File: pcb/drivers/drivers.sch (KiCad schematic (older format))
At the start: 19 parts, among them J1 Conn_01x04_Male, J2 Conn_01x04_Male, J3 Conn_01x04_Male, J4 Conn_01x04_Male, J5 Conn_01x04_Male, P1 Digital, P2 COM, P3 ADC, P4 Analog, P5 ADC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

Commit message: Polishing
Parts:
- added C2, C3: 0.1uF, Capacitor_SMD:C_0805_2012Metric_Pad1.18x1.45mm_HandSolder, symbol Device:C
- added J6: Conn_01x02_Male, TerminalBlock_Phoenix:TerminalBlock_Phoenix_MKDS-1,5-2_1x02_P5.00mm_Horizontal, symbol Connector:Conn_01x02_Male
- added Q5: IRLML6402, Package_TO_SOT_SMD:SOT-23, symbol Transistor_FET:IRLML6402
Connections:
- wire segments 81 -> 82
- no-connect marks 19 -> 18
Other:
- note added: "Power\n+5V"
- note added: "Reverse\npolarity\nprotection"
- moved on the sheet: C1
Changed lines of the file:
@@
 L Device:CP C1
 U 1 1 5FFF86DA
-P 7250 4175
-F 0 "C1" H 7368 4221 50  0000 L CNN
-F 1 "1000uF" H 7368 4130 50  0000 L CNN
-F 2 "Capacitor_THT:CP_Radial_D8.0mm_P2.50mm" H 7288 4025 50  0001 C CNN
-F 3 "~" H 7250 4175 50  0001 C CNN
-	1    7250 4175
+P 7000 5250
+F 0 "C1" H 7118 5296 50  0000 L CNN
+F 1 "1000uF" H 7118 5205 50  0000 L CNN
+F 2 "Capacitor_THT:CP_Radial_D8.0mm_P2.50mm" H 7038 5100 50  0001 C CNN
+F 3 "~" H 7000 5250 50  0001 C CNN
+	1    7000 5250
 	1    0    0    -1
 $EndComp
@@
 L power:GND #PWR016
 U 1 1 5FFF93FD
-P 7250 4325
-F 0 "#PWR016" H 7250 4075 50  0001 C CNN
-F 1 "GND" H 7255 4152 50  0000 C CNN
-F 2 "" H 7250 4325 50  0001 C CNN
-F 3 "" H 7250 4325 50  0001 C CNN
-	1    7250 4325
+P 7000 5400
+F 0 "#PWR016" H 7000 5150 50  0001 C CNN
+F 1 "GND" H 7005 5227 50  0000 C CNN
+F 2 "" H 7000 5400 50  0001 C CNN
+F 3 "" H 7000 5400 50  0001 C CNN
+	1    7000 5400
 	1    0    0    -1
 $EndComp
@@
 L power:VCC #PWR015
 U 1 1 5FFF9E1A
-P 7250 4025
-F 0 "#PWR015" H 7250 3875 50  0001 C CNN
-F 1 "VCC" H 7265 4198 50  0000 C CNN
-F 2 "" H 7250 4025 50  0001 C CNN
-F 3 "" H 7250 4025 50  0001 C CNN
-	1    7250 4025
+P 7000 5100
+F 0 "#PWR015" H 7000 4950 50  0001 C CNN
+F 1 "VCC" H 7015 5273 50  0000 C CNN
+F 2 "" H 7000 5100 50  0001 C CNN
+F 3 "" H 7000 5100 50  0001 C CNN
+	1    7000 5100
 	1    0    0    -1
 $EndComp
@@
 NoConn ~ 9000 2700
 NoConn ~ 9100 2300
-NoConn ~ 7600 3100
 NoConn ~ 9550 1000
 NoConn ~ 10350 1500
@@
 NoConn ~ 10050 3200
 NoConn ~ 9450 3225
+$Comp
+L Transistor_FET:IRLML6402 Q5
+U 1 1 5FF9B9AF
+P 7200 3850
+F 0 "Q5" V 7125 3900 50  0000 L CNN
+F 1 "IRLML6402" H 6850 3700 50  0000 L CNN
+F 2 "Package_TO_SOT_SMD:SOT-23" H 7400 3775 50  0001 L CIN
+F 3 "https://www.infineon.com/dgdl/irlml6402pbf.pdf?fileId=5546d462533600a401535668d5c2263c" H 7200 3850 50  0001 L CNN
+	1    7200 3850
+	0    -1   -1   0
+$EndComp
+$Comp
+L power:GND #PWR018
+U 1 1 5FFAC25B
+P 7200 4050
+F 0 "#PWR018" H 7200 3800 50  0001 C CNN
+F 1 "GND" H 7205 3877 50  0000 C CNN
+F 2 "" H 7200 4050 50  0001 C CNN
+F 3 "" H 7200 4050 50  0001 C CNN
+	1    7200 4050
+	1    0    0    -1
+$EndComp
+$Comp
+L Connector:Conn_01x02_Male J6
+U 1 1 5FFACF24
+P 6575 3750
+F 0 "J6" H 6683 3931 50  0000 C CNN
+F 1 "Conn_01x02_Male" H 6700 3475 50  0000 C CNN
+F 2 "TerminalBlock_Phoenix:TerminalBlock_Phoenix_MKDS-1,5-2_1x02_P5.00mm_Horizontal" H 6575 3750 50  0001 C CNN
+F 3 "~" H 6575 3750 50  0001 C CNN
+	1    6575 3750
+	1    0    0    -1
+$EndComp
+$Comp
+L power:GND #PWR017
+U 1 1 5FFADAD8
+P 6775 3850
+F 0 "#PWR017" H 6775 3600 50  0001 C CNN
+F 1 "GND" H 6900 3825 50  0000 C CNN
+F 2 "" H 6775 3850 50  0001 C CNN
+F 3 "" H 6775 3850 50  0001 C CNN
+	1    6775 3850
+	1    0    0    -1
+$EndComp
+Wire Wire Line
+	6775 3750 7000 3750
+Text Notes 6300 3875 0    50   ~ 0
+Power\n+5V
+Text Notes 7050 3550 0    50   ~ 0
+Reverse\npolarity\nprotection
+$Comp
+L power:VCC #PWR019
+U 1 1 5FFB386E
+P 7400 3750
+F 0 "#PWR019" H 7400 3600 50  0001 C CNN
+F 1 "VCC" V 7415 3878 50  0000 L CNN
+F 2 "" H 7400 3750 50  0001 C CNN
+F 3 "" H 7400 3750 50  0001 C CNN
+	1    7400 3750
+	0    1    1    0
+$EndComp
+$Comp
+L Device:C C2
+U 1 1 5FFF57D4
+P 7625 5250
+F 0 "C2" H 7740 5296 50  0000 L CNN
+F 1 "0.1uF" H 7740 5205 50  0000 L CNN
+F 2 "Capacitor_SMD:C_0805_2012Metric_Pad1.18x1.45mm_HandSolder" H 7663 5100 50  0001 C CNN
+F 3 "~" H 7625 5250 50  0001 C CNN
+	1    7625 5250
+	1    0    0    -1
+$EndComp
+$Comp
+L power:VCC #PWR020
+U 1 1 5FFF6495
+P 7625 5100
+F 0 "#PWR020" H 7625 4950 50  0001 C CNN
+F 1 "VCC" H 7640 5273 50  0000 C CNN
+F 2 "" H 7625 5100 50  0001 C CNN
+F 3 "" H 7625 5100 50  0001 C CNN
+	1    7625 5100
+	1    0    0    -1
+$EndComp
+$Comp
+L power:GND #PWR021
+U 1 1 5FFF6FB4
+P 7625 5400
+F 0 "#PWR021" H 7625 5150 50  0001 C CNN
+F 1 "GND" H 7630 5227 50  0000 C CNN
+F 2 "" H 7625 5400 50  0001 C CNN
+F 3 "" H 7625 5400 50  0001 C CNN
+	1    7625 5400
+	1    0    0    -1
+$EndComp
+$Comp
+L Device:C C3
+U 1 1 5FFF9188
+P 8250 5250
+F 0 "C3" H 8365 5296 50  0000 L CNN
+F 1 "0.1uF" H 8365 5205 50  0000 L CNN
+F 2 "Capacitor_SMD:C_0805_2012Metric_Pad1.18x1.45mm_HandSolder" H 8288 5100 50  0001 C CNN
+F 3 "~" H 8250 5250 50  0001 C CNN
+	1    8250 5250
+	1    0    0    -1
+$EndComp
+$Comp
+L power:VCC #PWR022
+U 1 1 5FFF918E
+P 8250 5100
+F 0 "#PWR022" H 8250 4950 50  0001 C CNN
+F 1 "VCC" H 8265 5273 50  0000 C CNN
+F 2 "" H 8250 5100 50  0001 C CNN
+F 3 "" H 8250 5100 50  0001 C CNN
+	1    8250 5100
+	1    0    0    -1
+$EndComp
+$Comp
+L power:GND #PWR023
+U 1 1 5FFF9194
+P 8250 5400
+F 0 "#PWR023" H 8250 5150 50  0001 C CNN
+F 1 "GND" H 8255 5227 50  0000 C CNN
+F 2 "" H 8250 5400 50  0001 C CNN
+F 3 "" H 8250 5400 50  0001 C CNN
+	1    8250 5400
+	1    0    0    -1
+$EndComp
 $EndSCHEMATC

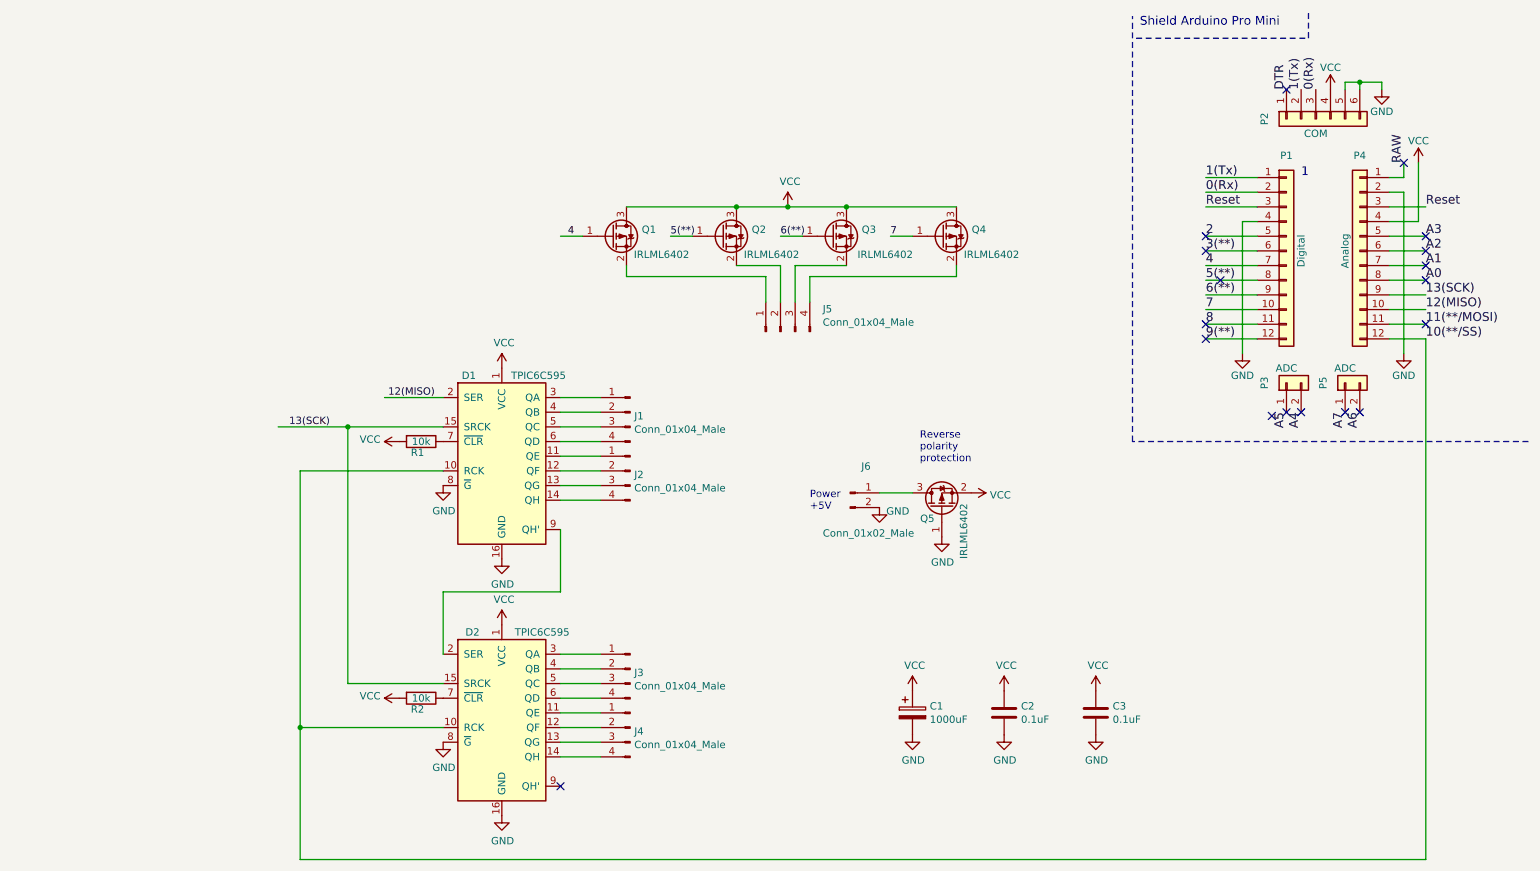
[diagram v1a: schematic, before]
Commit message: Replace Arduino Pro Mini to another Arduino Pro Mini
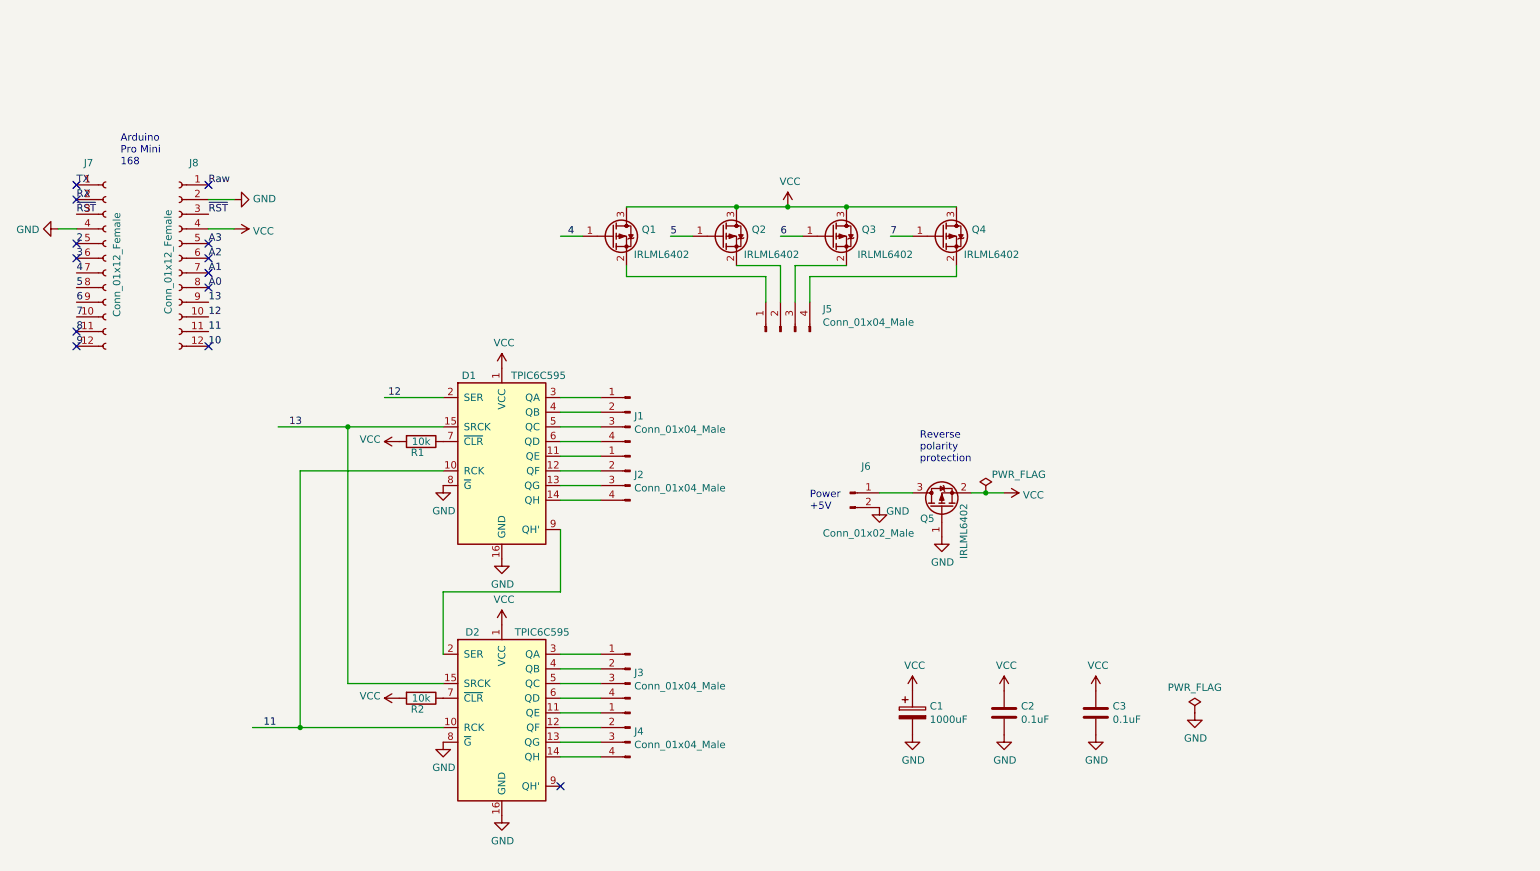
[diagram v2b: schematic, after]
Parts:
- removed P1: Digital, Socket_Arduino_Pro_Mini:Socket_Strip_Arduino_1x12, symbol Connector_Generic:Conn_01x12
- removed P2: COM, Socket_Arduino_Pro_Mini:Socket_Strip_Arduino_1x06, symbol Connector_Generic:Conn_01x06
- removed P3, P5: ADC, Socket_Arduino_Pro_Mini:Socket_Strip_Arduino_1x02, symbol Connector_Generic:Conn_01x02
- removed P4: Analog, Socket_Arduino_Pro_Mini:Socket_Strip_Arduino_1x12, symbol Connector_Generic:Conn_01x12
- added J7, J8: Conn_01x12_Female, Connector_PinSocket_2.54mm:PinSocket_1x12_P2.54mm_Vertical, symbol Connector:Conn_01x12_Female
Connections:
- net labels added: 10, 11, 12, 13, 3, 5, 6, 9, RX, Raw, TX, ~RST
- net labels removed: 0(Rx), 1(Tx), 10(**/SS), 11(**/MOSI), 12(MISO), 13(SCK), 3(**), 5(**), 6(**), 9(**), A4, A5, A6, A7, DTR, RAW, Reset
- wire segments 82 -> 52
- no-connect marks 18 -> 13
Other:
- note added: "Arduino\nPro Mini\n168"
- note removed: "1"
- note removed: "Shield Arduino Pro Mini \n"

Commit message: Swap pin 12 and 13
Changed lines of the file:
@@
 $EndComp
 Text Label 3425 3100 0    50   ~ 0
-12
+13
 Wire Wire Line
 	3800 3100 3400 3100
@@
 	3800 3300 3150 3300
 Text Label 2750 3300 0    50   ~ 0
-13
+12
 Wire Wire Line
 	3800 5050 3150 5050

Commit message: Polishing
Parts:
- added H1, H2, H3, H4, H5: MountingHole, MountingHole:MountingHole_3.2mm_M3, symbol Mechanical:MountingHole
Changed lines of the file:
@@
+	1    0    0    -1
+$EndComp
+$Comp
+L Mechanical:MountingHole H1
+U 1 1 5FFB46E8
+P 8500 1500
+F 0 "H1" H 8600 1546 50  0000 L CNN
+F 1 "MountingHole" H 8600 1455 50  0000 L CNN
+F 2 "MountingHole:MountingHole_3.2mm_M3" H 8500 1500 50  0001 C CNN
+F 3 "~" H 8500 1500 50  0001 C CNN
+	1    8500 1500
+	1    0    0    -1
+$EndComp
+$Comp
+L Mechanical:MountingHole H2
+U 1 1 5FFB5433
+P 8500 2000
+F 0 "H2" H 8600 2046 50  0000 L CNN
+F 1 "MountingHole" H 8600 1955 50  0000 L CNN
+F 2 "MountingHole:MountingHole_3.2mm_M3" H 8500 2000 50  0001 C CNN
+F 3 "~" H 8500 2000 50  0001 C CNN
+	1    8500 2000
+	1    0    0    -1
+$EndComp
+$Comp
+L Mechanical:MountingHole H3
+U 1 1 5FFCCF1D
+P 8500 2500
+F 0 "H3" H 8600 2546 50  0000 L CNN
+F 1 "MountingHole" H 8600 2455 50  0000 L CNN
+F 2 "MountingHole:MountingHole_3.2mm_M3" H 8500 2500 50  0001 C CNN
+F 3 "~" H 8500 2500 50  0001 C CNN
+	1    8500 2500
+	1    0    0    -1
+$EndComp
+$Comp
+L Mechanical:MountingHole H4
+U 1 1 5FFE3C58
+P 8500 3000
+F 0 "H4" H 8600 3046 50  0000 L CNN
+F 1 "MountingHole" H 8600 2955 50  0000 L CNN
+F 2 "MountingHole:MountingHole_3.2mm_M3" H 8500 3000 50  0001 C CNN
+F 3 "~" H 8500 3000 50  0001 C CNN
+	1    8500 3000
+	1    0    0    -1
+$EndComp
+$Comp
+L Mechanical:MountingHole H5
+U 1 1 5FFF9599
+P 8500 3500
+F 0 "H5" H 8600 3546 50  0000 L CNN
+F 1 "MountingHole" H 8600 3455 50  0000 L CNN
+F 2 "MountingHole:MountingHole_3.2mm_M3" H 8500 3500 50  0001 C CNN
+F 3 "~" H 8500 3500 50  0001 C CNN
+	1    8500 3500
 	1    0    0    -1
 $EndComp
